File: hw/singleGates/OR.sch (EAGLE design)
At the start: 8 parts, among them Q1 BC817, Q2 BC817, Q3 BC817

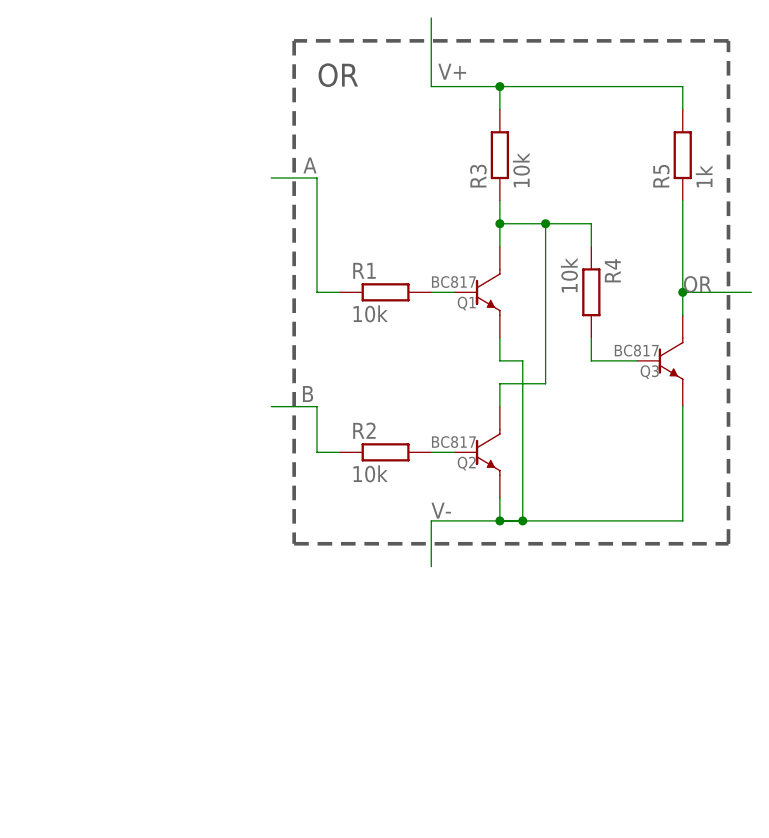
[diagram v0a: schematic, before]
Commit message: Updated gates to be centered
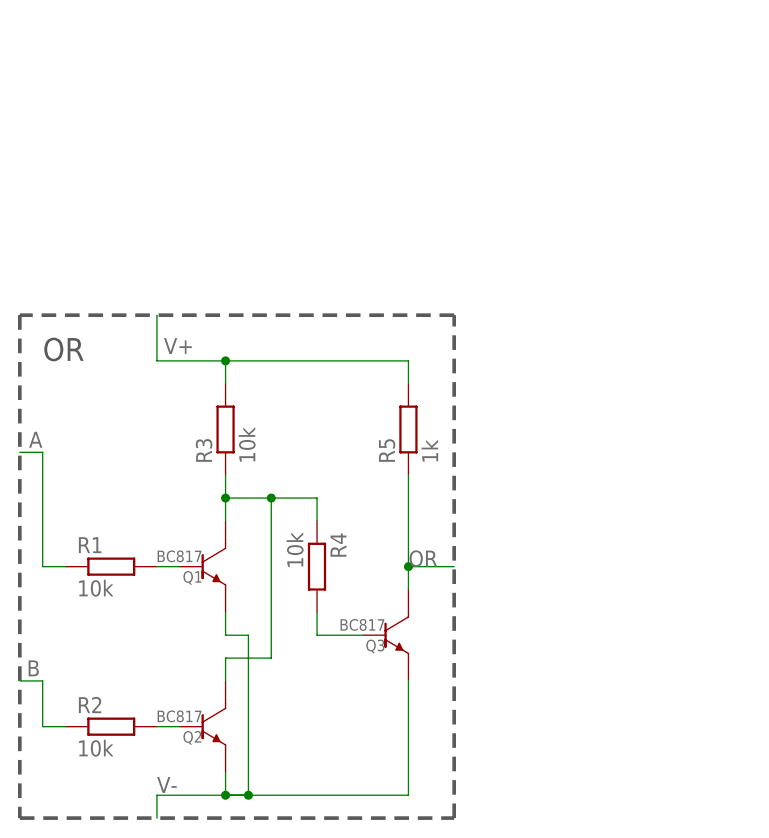
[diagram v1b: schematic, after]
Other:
- moved on the sheet: Q1, Q2, Q3, R1, R2, R3, R4, R5

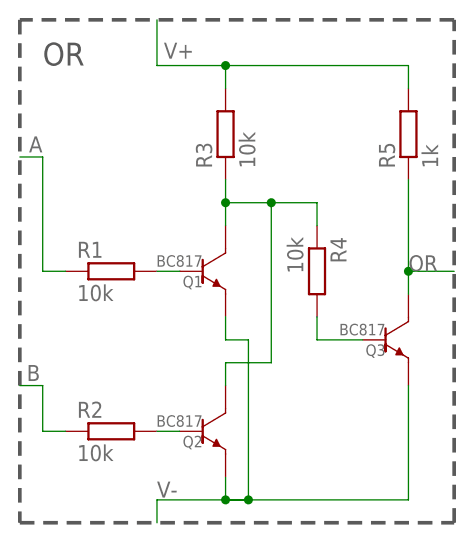
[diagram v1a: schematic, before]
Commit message: Updated supply line names to be more spice compatible
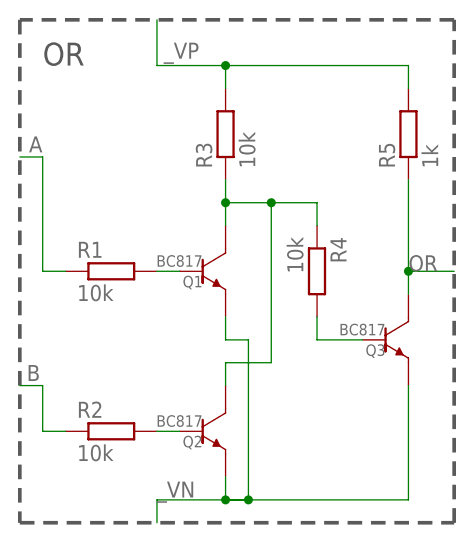
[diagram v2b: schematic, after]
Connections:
- net V+ renamed _VP
- net V- renamed _VN
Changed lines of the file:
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@@
 <?xml version="1.0" encoding="utf-8"?>
 <!DOCTYPE eagle SYSTEM "eagle.dtd">
-<eagle version="7.4.0">
+<eagle version="7.3.0">
 <drawing>
 <settings>
@@
 </segment>
 </net>
-<net name="V-" class="0">
+<net name="_VN" class="0">
 <segment>
 <wire x1="-5.08" y1="-25.4" x2="-5.08" y2="-22.86" width="0.1524" layer="91"/>
@@
 </segment>
 </net>
-<net name="V+" class="0">
+<net name="_VP" class="0">
 <segment>
 <pinref part="R3" gate="G$1" pin="2"/>
